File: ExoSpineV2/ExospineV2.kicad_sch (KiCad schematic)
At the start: 10 parts, among them J1 GPIO, J4 Conn_01x03_Socket, J5 Conn_01x04_Socket, U1 CAT24C256

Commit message: jsp ce que j'ai fait mais j'ai avancé
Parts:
- added J2: Conn_01x03_Pin, symbol Connector:Conn_01x03_Pin
- J5: footprint (none) -> Connector_PinSocket_2.00mm:PinSocket_1x04_P2.00mm_Vertical
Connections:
- net +3V3: now also J2.3 (Pin_3)
- net GND: now also J2.1 (Pin_1)
- net GPIO14/TXD0: now also J2.2 (Pin_2)
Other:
- removed sheet ExoSpineV1
- note added: "GPS connector"
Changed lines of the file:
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@@
     (stroke (width 0) (type solid))
+  )
+  (wire (pts (xy 173.99 143.51) (xy 177.8 143.51))
+    (stroke (width 0) (type default))
   )
   (wire (pts (xy 76.2 63.5) (xy 76.2 68.58))
@@
     (stroke (width 0) (type solid))
   )
+  (wire (pts (xy 173.99 140.97) (xy 173.99 143.51))
+    (stroke (width 0) (type default))
+  )
   (wire (pts (xy 52.07 111.76) (xy 22.86 111.76))
     (stroke (width 0) (type solid))
@@
     (stroke (width 0) (type solid))
   )
+  (wire (pts (xy 177.8 148.59) (xy 173.99 148.59))
+    (stroke (width 0) (type default))
+  )
   (wire (pts (xy 73.66 71.12) (xy 100.33 71.12))
     (stroke (width 0) (type solid))
@@
     (stroke (width 0) (type default))
   )
+  (wire (pts (xy 173.99 148.59) (xy 173.99 152.4))
+    (stroke (width 0) (type default))
+  )
   (wire (pts (xy 130.81 38.1) (xy 147.32 38.1))
     (stroke (width 0) (type default))
@@
     (stroke (width 0) (type default))
   )
+  (wire (pts (xy 162.56 146.05) (xy 177.8 146.05))
+    (stroke (width 0) (type default))
+  )
   (wire (pts (xy 76.2 68.58) (xy 76.2 80.01))
     (stroke (width 0) (type solid))
@@
   (wire (pts (xy 73.66 60.96) (xy 100.33 60.96))
     (stroke (width 0) (type solid))
+  )
+  (rectangle (start 160.02 134.62) (end 208.28 161.29)
+    (stroke (width 0) (type default))
+    (fill (type none))
   )
   (rectangle (start 160.02 107.95) (end 207.01 133.35)
@@
     (effects (font (size 1.27 1.27)) (justify left bottom))
   )
+  (text "GPS connector\n" (at 187.96 137.16 0)
+    (effects (font (size 1.27 1.27)) (justify left bottom))
+  )
   (label "ID_SDA" (at 31.75 60.96 0) (fields_autoplaced)
     (effects (font (size 1.27 1.27)) (justify left bottom))
@@
   (label "GPIO7{slash}SPI0.CE1" (at 100.33 58.42 180) (fields_autoplaced)
     (effects (font (size 1.27 1.27)) (justify right bottom))
+  )
+  (label "GPIO14{slash}TXD0" (at 162.56 146.05 0) (fields_autoplaced)
+    (effects (font (size 1.27 1.27)) (justify left bottom))
   )
   (label "GPIO3{slash}SDA1" (at 161.29 124.46 0) (fields_autoplaced)
@@
     )
   )
+  (symbol (lib_name "GND_3") (lib_id "power:GND") (at 173.99 152.4 0) (unit 1)
+    (in_bom yes) (on_board yes) (dnp no) (fields_autoplaced)
+    (property "Reference" "#PWR025" (at 173.99 158.75 0)
+      (effects (font (size 1.27 1.27)) hide)
+    )
+    (property "Value" "GND" (at 173.99 157.48 0)
+      (effects (font (size 1.27 1.27)))
+    )
+    (property "Footprint" "" (at 173.99 152.4 0)
+      (effects (font (size 1.27 1.27)) hide)
+    )
+    (property "Datasheet" "" (at 173.99 152.4 0)
+      (effects (font (size 1.27 1.27)) hide)
+    )
+    (pin "1")
+    (instances
+      (project "ExospineV2"
+        (path "/e63e39d7-6ac0-4ffd-8aa3-1841a4541b55"
+          (reference "#PWR025") (unit 1)
+        )
+      )
+    )
+  )
   (symbol (lib_id "Device:C_Small") (at 67.31 177.8 0) (unit 1)
     (in_bom yes) (on_board yes) (dnp no)
@@
     )
   )
+  (symbol (lib_id "power:+12V") (at 208.28 68.58 0) (unit 1)
+    (in_bom yes) (on_board yes) (dnp no) (fields_autoplaced)
+    (property "Reference" "#PWR023" (at 208.28 72.39 0)
+      (effects (font (size 1.27 1.27)) hide)
+    )
+    (property "Value" "+12V" (at 208.28 63.5 0)
+      (effects (font (size 1.27 1.27)))
+    )
+    (property "Footprint" "" (at 208.28 68.58 0)
+      (effects (font (size 1.27 1.27)) hide)
+    )
+    (property "Datasheet" "" (at 208.28 68.58 0)
+      (effects (font (size 1.27 1.27)) hide)
+    )
+    (pin "1")
+    (instances
+      (project "ExospineV2"
+        (path "/e63e39d7-6ac0-4ffd-8aa3-1841a4541b55"
+          (reference "#PWR023") (unit 1)
+        )
+      )
+    )
+  )
+  (symbol (lib_id "Connector:Conn_01x03_Pin") (at 182.88 146.05 180) (unit 1)
+    (in_bom yes) (on_board yes) (dnp no) (fields_autoplaced)
+    (property "Reference" "J2" (at 184.15 144.78 0)
+      (effects (font (size 1.27 1.27)) (justify right))
+    )
+    (property "Value" "Conn_01x03_Pin" (at 184.15 147.32 0)
+      (effects (font (size 1.27 1.27)) (justify right))
+    )
+    (property "Footprint" "" (at 182.88 146.05 0)
+      (effects (font (size 1.27 1.27)) hide)
+    )
+    (property "Datasheet" "~" (at 182.88 146.05 0)
+      (effects (font (size 1.27 1.27)) hide)
+    )
+    (pin "1")
+    (pin "2")
+    (pin "3")
+    (instances
+      (project "ExospineV2"
+        (path "/e63e39d7-6ac0-4ffd-8aa3-1841a4541b55"
+          (reference "J2") (unit 1)
+        )
+      )
+    )
+  )
   (symbol (lib_id "power:+3.3V") (at 127 38.1 0) (unit 1)
     (in_bom yes) (on_board yes) (dnp no)
@@
     )
   )
+  (symbol (lib_id "power:+3.3V") (at 173.99 140.97 0) (unit 1)
+    (in_bom yes) (on_board yes) (dnp no)
+    (property "Reference" "#PWR024" (at 173.99 144.78 0)
+      (effects (font (size 1.27 1.27)) hide)
+    )
+    (property "Value" "+3.3V" (at 174.3583 136.6456 0)
+      (effects (font (size 1.27 1.27)))
+    )
+    (property "Footprint" "" (at 173.99 140.97 0)
+      (effects (font (size 1.27 1.27)))
+    )
+    (property "Datasheet" "" (at 173.99 140.97 0)
+      (effects (font (size 1.27 1.27)))
+    )
+    (pin "1")
+    (instances
+      (project "ExospineV2"
+        (path "/e63e39d7-6ac0-4ffd-8aa3-1841a4541b55"
+          (reference "#PWR024") (unit 1)
+        )
+      )
+    )
+  )
   (symbol (lib_id "power:GND") (at 81.28 190.5 0) (unit 1)
     (in_bom yes) (on_board yes) (dnp no)
@@
       (effects (font (size 1.27 1.27)))
     )
-    (property "Footprint" "" (at 184.15 119.38 0)
+    (property "Footprint" "Connector_PinSocket_2.00mm:PinSocket_1x04_P2.00mm_Vertical" (at 184.15 119.38 0)
       (effects (font (size 1.27 1.27)) hide)
     )
@@
     )
   )
-  (sheet (at 193.04 55.88) (size 13.97 3.81) (fields_autoplaced)
-    (stroke (width 0.1524) (type solid))
-    (fill (color 0 0 0 0.0000))
-    (property "Sheetname" "ExoSpineV1" (at 193.04 55.1684 0)
-      (effects (font (size 1.27 1.27)) (justify left bottom))
-    )
-    (property "Sheetfile" "ExoSpineV1.kicad_sch" (at 193.04 60.2746 0)
-      (effects (font (size 1.27 1.27)) (justify left top))
-    )
-    (instances
-      (project "ExospineV2"
-        (path "/e63e39d7-6ac0-4ffd-8aa3-1841a4541b55" (page "2"))
-      )
-    )
-  )
-  (sheet (at 52.07 109.22) (size 17.78 11.43) (fields_autoplaced)
+  (sheet (at 52.07 109.22) (size 17.78 12.7) (fields_autoplaced)
     (stroke (width 0.1524) (type solid))
     (fill (color 0 0 0 0.0000))
@@
       (effects (font (size 1.27 1.27)) (justify left bottom))
     )
-    (property "Sheetfile" "MCP3008.kicad_sch" (at 52.07 121.2346 0)
+    (property "Sheetfile" "MCP3008.kicad_sch" (at 52.07 122.5046 0)
       (effects (font (size 1.27 1.27)) (justify left top))
     )

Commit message: organized
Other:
- added sheet ExoSpineV1 (ExoSpineV1.kicad_sch)
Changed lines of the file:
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@@
+    )
+  )
+  (sheet (at 124.46 109.22) (size 12.7 3.81) (fields_autoplaced)
+    (stroke (width 0.1524) (type solid))
+    (fill (color 0 0 0 0.0000))
+    (property "Sheetname" "ExoSpineV1" (at 124.46 108.5084 0)
+      (effects (font (size 1.27 1.27)) (justify left bottom))
+    )
+    (property "Sheetfile" "ExoSpineV1.kicad_sch" (at 124.46 113.6146 0)
+      (effects (font (size 1.27 1.27)) (justify left top))
+    )
+    (instances
+      (project "ExospineV2"
+        (path "/e63e39d7-6ac0-4ffd-8aa3-1841a4541b55" (page "4"))
+      )
     )
   )

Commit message: Temperature Sensor 1
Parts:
- removed C1: 100n, symbol Device:C_Small
- removed JP1: ID_WP, symbol Jumper:SolderJumper_2_Open
- removed R1, R2: 3.9k, symbol Device:R_Small
- removed U1: CAT24C256, symbol Memory_EEPROM:CAT24C256
- added C27, C28, C29, C30, C31, C32, C33, C34: 1µF, symbol Device:C
- added J20, J21, J22, J23: S2B-PH-K-S(LF)(SN), Connector_PinHeader_2.00mm:PinHeader_1x02_P2.00mm_Vertical, symbol Connector:Conn_01x02_Pin
- added Q6, Q7: Q_NMOS_DGS, symbol Device:Q_NMOS_DGS
- added R20, R21: 10k, symbol Device:R
- added R22: 1k, symbol Device:R
- added R23: 2.2k, symbol Device:R
- added U6: MCP3008, symbol Analog_ADC:MCP3008
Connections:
- net GND: now also C27.2, C28.2, C29.2, C30.2, C31.2, C32.2, C33.2, C34.2, R22.1, U6.14 (AGND), U6.9 (DGND)
- new net: Q6.3 (S), Q7.3 (S), R20.2, R21.2
- new net: R23.2, U6.12 (Dout)
- new net: C33.1, J20.1 (Pin_1), U6.7 (CH6)
- new net: C34.1, J20.2 (Pin_2), U6.8 (CH7)
- new net: R22.2, R23.1
- new net 5V: U6.15 (Vref), U6.16 (Vdd)
- new net CS/SHDN: U6.10 (~{CS}/SHDN)
- new net Channel0: C27.1, J23.1 (Pin_1), U6.1 (CH0)
- new net Channel1: C28.1, J23.2 (Pin_2), U6.2 (CH1)
- new net Channel2: C29.1, J22.1 (Pin_1), U6.3 (CH2)
- new net Channel3: C30.1, J22.2 (Pin_2), U6.4 (CH3)
- new net Channel4: C31.1, J21.1 (Pin_1), U6.5 (CH4)
- new net Channel5: C32.1, J21.2 (Pin_2), U6.6 (CH5)
- new net GPIO12: Q6.2 (G), R20.1
- new net GPIO19: Q7.2 (G), R21.1
- new net SPI_Click: U6.13 (CLK)
- new net SPI_MOSI: U6.11 (Din)
- no-connect marks 3 -> 28
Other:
- note added: "GPS"
- note removed: "GPS connector"
- note removed: "ID_SD and ID_SC PINS: These pins are reserved for HAT ID EEPROM. At boot time this I2C interface will be interrogated to look for an EEPROM that identifes the attached board and allows automagic setup of the GPIOs (and optionally, Linux drivers). Bridging JP1 enables write protection. DO NOT USE these pins for anything other than attaching an I2C ID EEPROM. Leave unconnected if ID EEPROM not requ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"
- note removed: "Thermistances"
- moved on the sheet: C26, J2, J4, J5, R3

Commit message: Added actuators logic circuits
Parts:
- removed J2: Conn_01x03_Pin, symbol Connector:Conn_01x03_Pin
- removed J4: Conn_01x03_Socket, Connector_JST:JST_EH_B3B-EH-A_1x03_P2.50mm_Vertical, symbol Connector:Conn_01x03_Socket
- removed J5: Conn_01x04_Socket, Connector_PinSocket_2.00mm:PinSocket_1x04_P2.00mm_Vertical, symbol Connector:Conn_01x04_Socket
- added J24: Conn_01x02, symbol Connector_Generic:Conn_01x02
- added J25, J26, J28, J29: Conn_01x03, symbol Connector_Generic:Conn_01x03
- added J27: Conn_01x04, symbol Connector_Generic:Conn_01x04
- added U8: ~, symbol ExoSpine_CustomLibrary:ActuatorsFeedback_LogicCircuit
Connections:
- net +3V3: now also J25.1 (Pin_1), J26.1 (Pin_1); no longer J1.1 (Pin_1), J1.17 (Pin_17)
- net +5V: now also J27.1 (Pin_1); no longer J1.2 (Pin_2), J1.4 (Pin_4)
- net 5V: now also J1.2 (Pin_2), J1.4 (Pin_4)
- net GND: now also J25.3 (Pin_3), J26.3 (Pin_3), J27.2 (Pin_2)
- net GPIO14/TXD0: now also J26.2 (Pin_2)
- net GPIO17: now also J25.2 (Pin_2)
- net GPIO2/SCL1: now also J27.3 (Pin_3)
- net GPIO3/SDA1: now also J27.4 (Pin_4)
- new net: J29.2 (Pin_2), U8.2 (B)
- new net: J29.3 (Pin_3), U8.1 (A)
- new net 3.3V: J1.1 (Pin_1), J1.17 (Pin_17), J29.1 (Pin_1)
- new net GPIO: U8.3 (X)
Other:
- note added: "Actuator 1 Feedback"
- note added: "Button"
- note added: "Contactors"
- note added: "Temperature Sensor 1"
- note removed: "Additional pin functions: https://pinout.xyz/"
- moved on the sheet: Q6, Q7, R20, R21

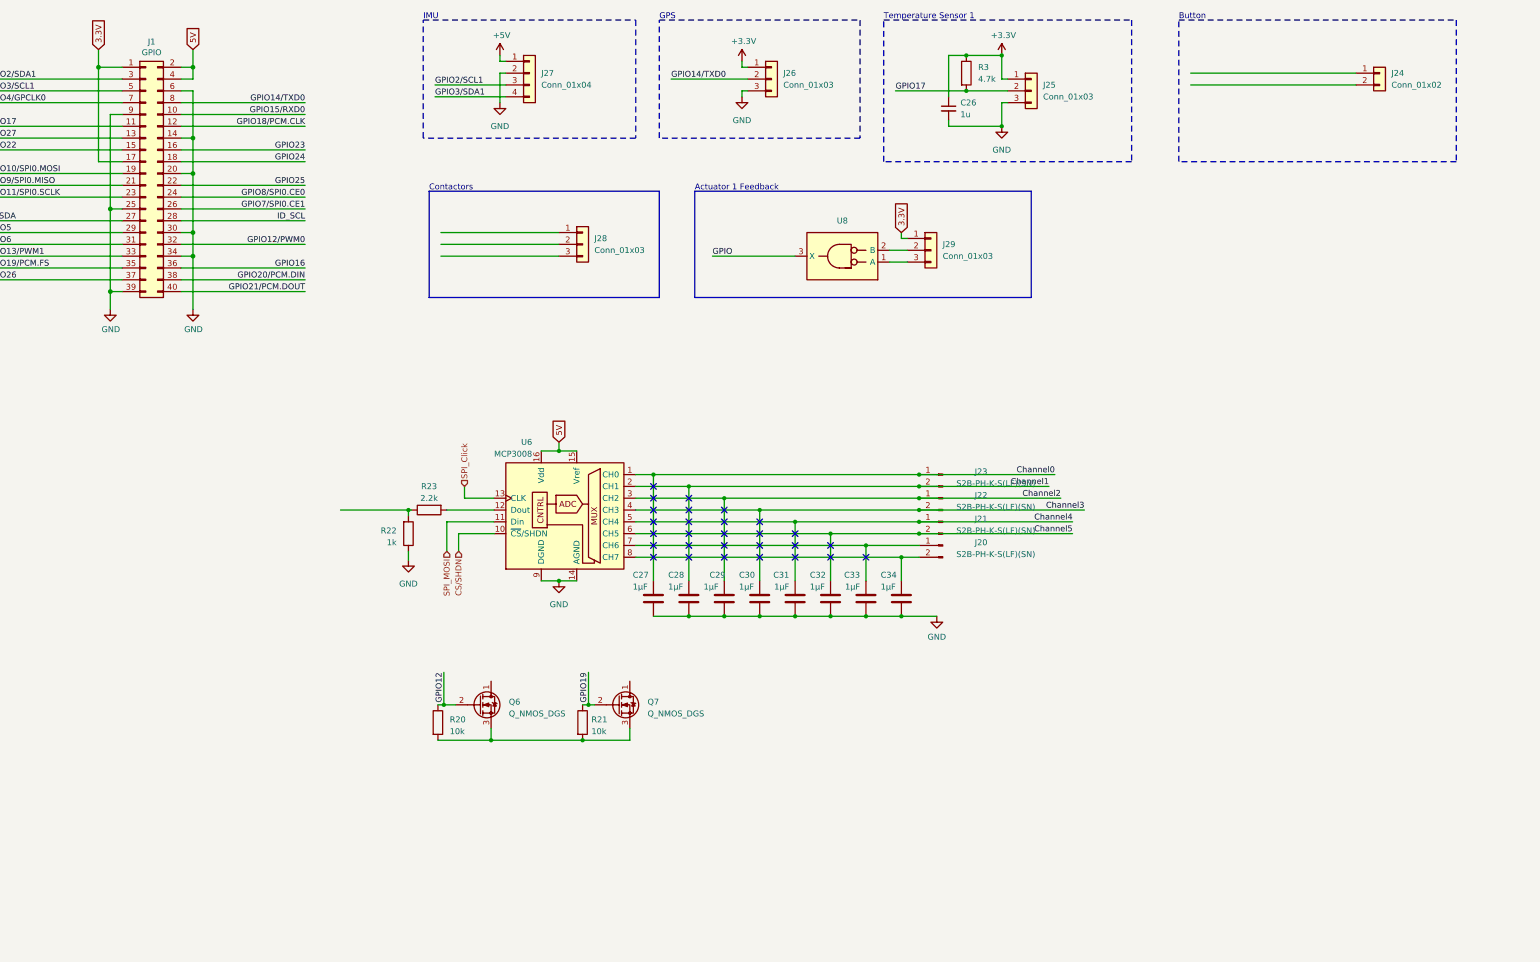
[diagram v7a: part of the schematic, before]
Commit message: modified actuators
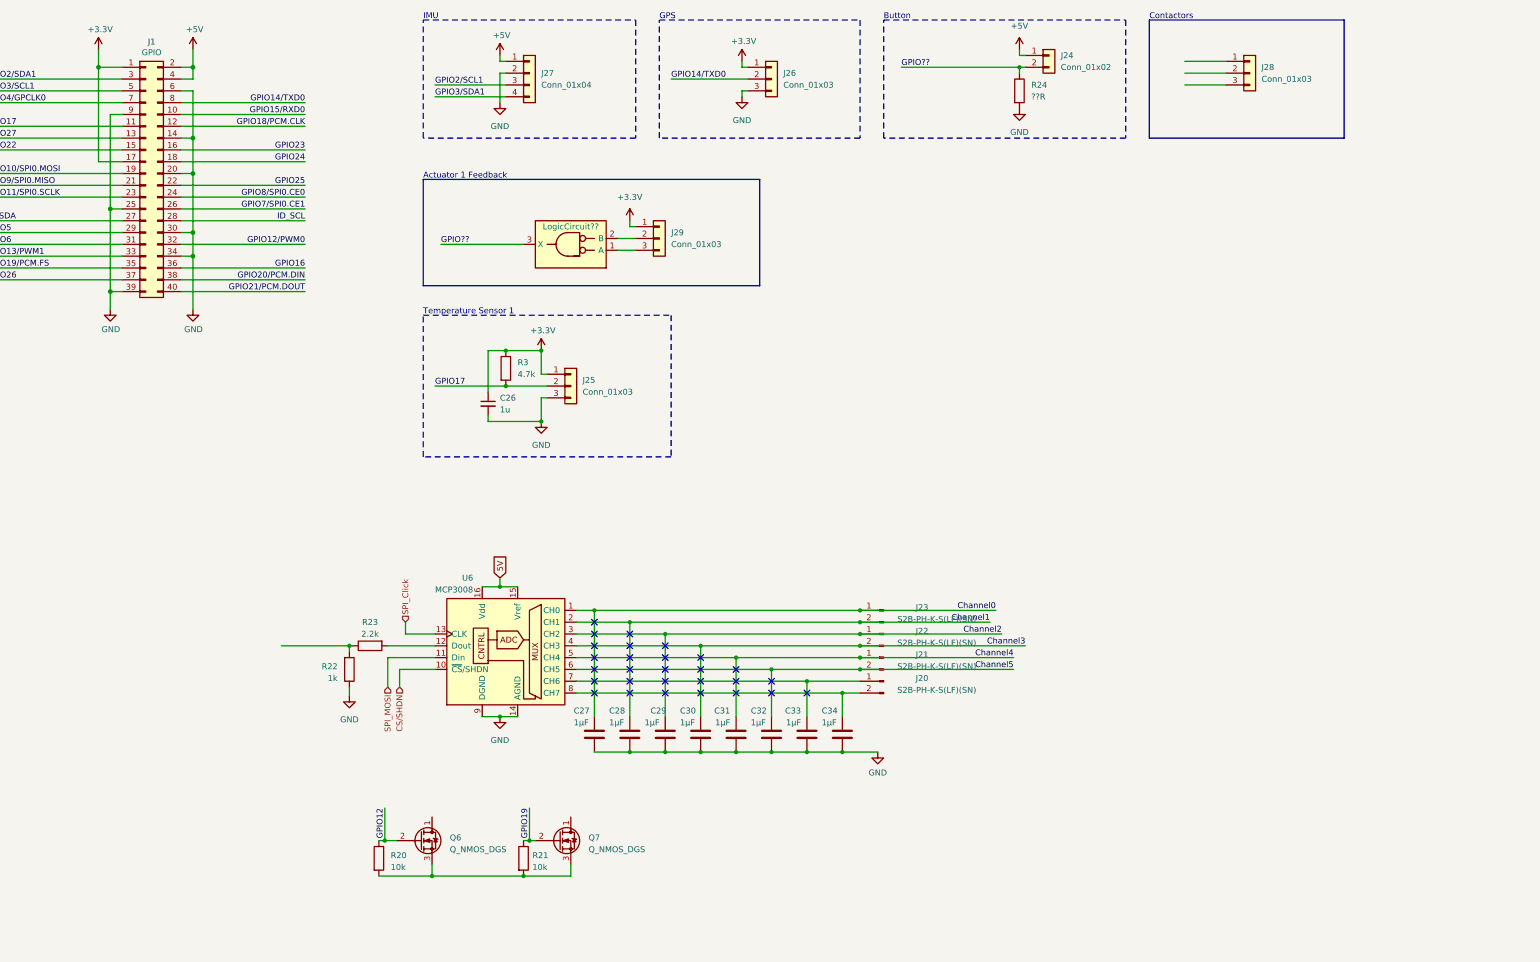
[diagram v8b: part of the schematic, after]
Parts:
- added R24: ??R, symbol Device:R
- renumbered U8 to LogicCircuit??
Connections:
- net GPIO is gone; now on net GPIO??: LogicCircuit??.3 (X)
- net +3V3: now also J1.1 (Pin_1), J1.17 (Pin_17)
- net +5V: now also J1.2 (Pin_2), J1.4 (Pin_4), J24.1 (Pin_1)
- net 5V: no longer J1.2 (Pin_2), J1.4 (Pin_4)
- net GND: now also R24.2
- net GPIO??: now reaches J24.2 (Pin_2)
- net GPIO??: now also R24.1
- removed net 3.3V: J1.1 (Pin_1), J1.17 (Pin_17), J29.1 (Pin_1)
- new net +3.3V: J29.1 (Pin_1)
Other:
- moved on the sheet: C26, C27, C28, C29, C30, C31, C32, C33, C34, J20, J21, J22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
